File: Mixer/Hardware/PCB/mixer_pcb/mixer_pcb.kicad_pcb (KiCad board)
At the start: 2 copper layers, 40 x 100 mm, 38 parts, among them J1 THONKICONN, J2 THONKICONN, J3 THONKICONN, J4 THONKICONN, J5 THONKICONN, J6 THONKICONN, J7 Eurorack_2x5_Power, J8 Conn_01x02_Socket, J9 Conn_01x02_Socket, SW1 TAIWAY 200CWMSP1T3B4M2, SW2 TAIWAY 200CWMSP1T3B4M2, SW3 TAIWAY 200CWMSP1T3B4M2, SW4 TAIWAY 200CWMSP1T3B4M2, SW5 TAIWAY 200CWMSP1T3B4M2, U1 Opamp_Dual

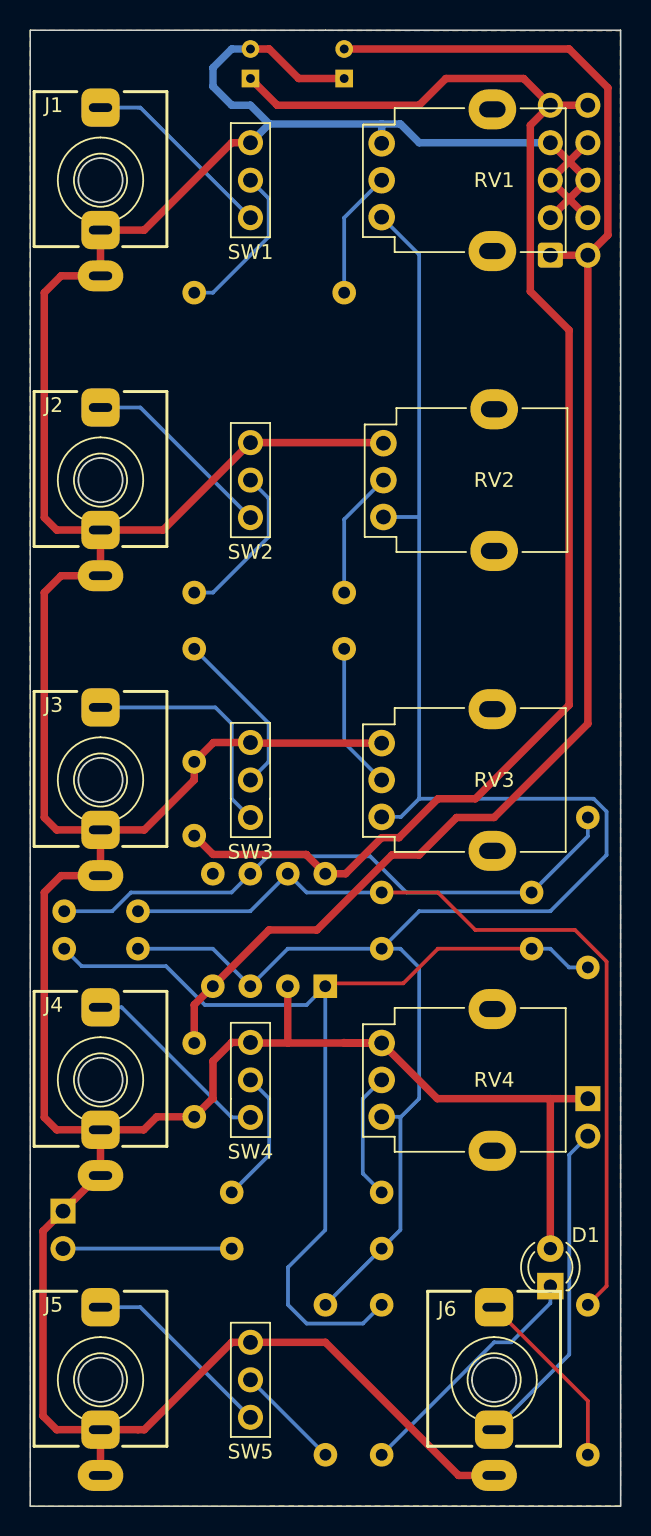
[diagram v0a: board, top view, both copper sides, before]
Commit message: Fix some bugs in the new Mixer PCB
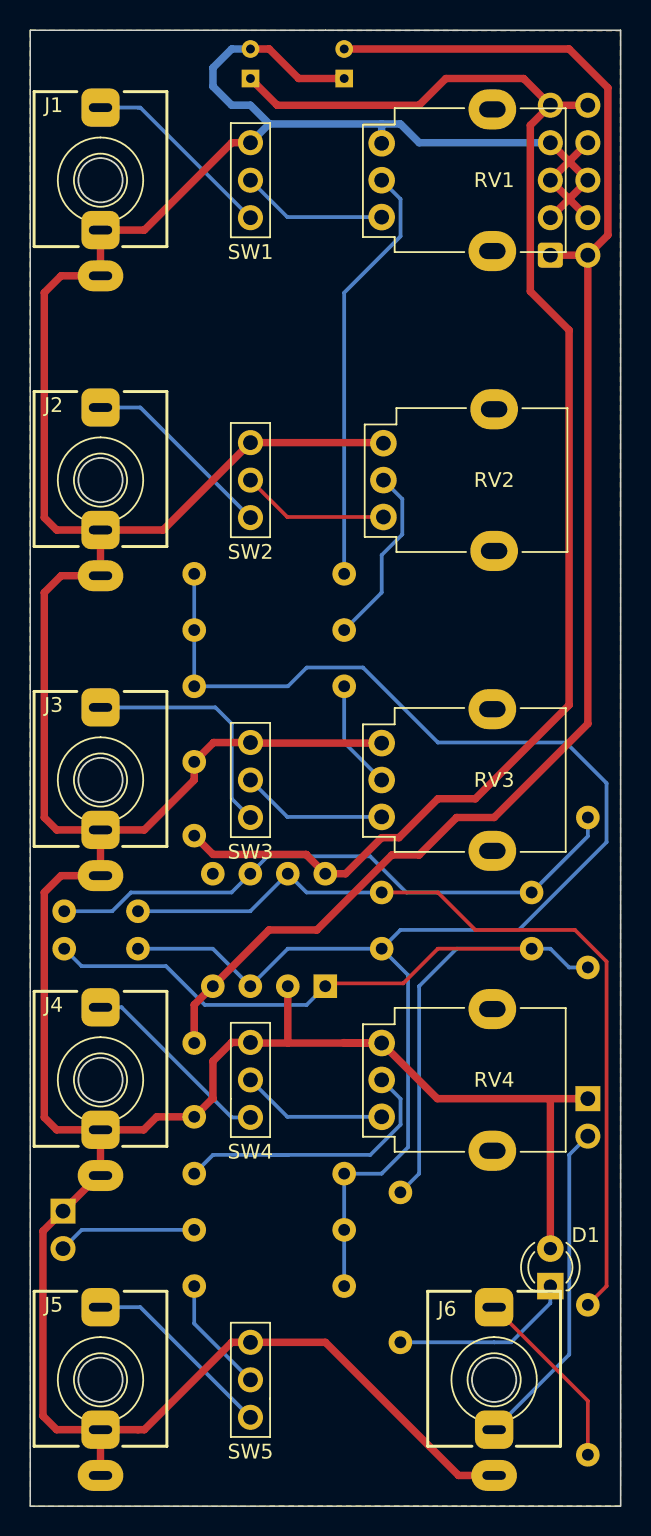
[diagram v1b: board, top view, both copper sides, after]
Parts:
- moved R1 21.6 mm to (77.5, 62.2), turned to 180 degrees
- moved R5 14.5 mm to (67.3, 110.5), turned to 0 degrees
- moved R2 10.5 mm to (77.5, 66.0), turned to 180 degrees
- moved R3 10.5 mm to (77.5, 69.8), turned to 180 degrees
- moved R11 7.73 mm to (81.3, 114.3)
- moved R4 2.84 mm to (67.3, 102.9)
- moved R6 2.84 mm to (67.3, 106.7)
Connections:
- R1 pad 1: Net-(SW1-B) -> Net-(R1-Pad1)
- R1 pad 2: Net-(R1-Pad2) -> Net-(U1A-+)
- R2 pad 1: Net-(SW2-B) -> Net-(R2-Pad1)
- R2 pad 2: Net-(R2-Pad2) -> Net-(U1A-+)
- R3 pad 1: Net-(SW3-B) -> Net-(R3-Pad1)
- R3 pad 2: Net-(R3-Pad2) -> Net-(U1A-+)
- R4 pad 1: Net-(SW4-B) -> Net-(R4-Pad1)
- R4 pad 2: Net-(R4-Pad2) -> Net-(U1A-+)
- RV1 pad 2: Net-(R1-Pad2) -> Net-(R1-Pad1)
- RV1 pad 3: Net-(U1A-+) -> Net-(SW1-B)
- RV2 pad 2: Net-(R2-Pad2) -> Net-(R2-Pad1)
- RV2 pad 3: Net-(U1A-+) -> Net-(SW2-B)
- RV3 pad 2: Net-(R3-Pad2) -> Net-(R3-Pad1)
- RV3 pad 3: Net-(U1A-+) -> Net-(SW3-B)
- RV4 pad 2: Net-(R4-Pad2) -> Net-(R4-Pad1)
- RV4 pad 3: Net-(U1A-+) -> Net-(SW4-B)
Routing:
- net Net-(R1-Pad1): track 0.00 -> 28.8 mm
- net Net-(U1A-+): track 128.3 -> 107.1 mm
- net Net-(R4-Pad1): track 0.00 -> 20.2 mm
- net Net-(R2-Pad1): track 0.00 -> 12.3 mm
- net Net-(R3-Pad2): track 9.94 -> 0.00 mm
- net Net-(R2-Pad2): track 8.72 -> 0.00 mm
- net Net-(R4-Pad2): track 8.68 -> 0.00 mm
- net Net-(R1-Pad2): track 8.67 -> 0.00 mm
- net Net-(R3-Pad1): track 0.00 -> 7.40 mm
- net Net-(C3-Pad2): track 69.2 -> 62.3 mm
- net Net-(D1-K): track 16.8 -> 12.4 mm
- net Net-(J8-Pin_2): track 11.4 -> 9.42 mm
- net Net-(SW3-B): track 11.5 -> 9.93 mm
- net Net-(SW1-B): track 11.0 -> 9.93 mm
- net Net-(SW2-B): track 11.0 -> 10.0 mm
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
